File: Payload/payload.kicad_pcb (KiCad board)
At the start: 4 copper layers, 90 x 40 mm, 85 parts, among them J1 Conn_ARM_JTAG_SWD_10, J2 Conn_01x02, J3 Conn_01x03, Q1 Q_PMOS_GSD, SW1 SW_SPST, U1 STM32L471RGTx, U2 ISO1541, U3 MAX6371, U4 CY62167EV30LL, U5 CY62167EV30LL, U6 CY62167EV30LL, U7 CY62167EV30LL, Y1 8 MHz

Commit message: Partial routing
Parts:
- moved C13 1.25 mm to (127.2, 80.0)
- moved C14 1.25 mm to (102.2, 102.0)
- moved C15 1.25 mm to (127.2, 102.0)
- moved C9 1.25 mm to (102.2, 80.0)
- moved U4 1.25 mm to (114.2, 79.0)
- moved U5 1.25 mm to (139.2, 79.0)
- moved U6 1.25 mm to (114.2, 101.0)
- moved U7 1.25 mm to (139.2, 101.0)
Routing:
- net /A1: track 0.00 -> 126.9 mm, vias 0 -> 5
- net /A2: track 0.00 -> 125.6 mm, vias 0 -> 5
- net /A3: track 0.00 -> 123.2 mm, vias 0 -> 5
- net /A4: track 0.00 -> 120.5 mm, vias 0 -> 5
- net /A5: track 0.00 -> 117.7 mm, vias 0 -> 5
- net /A6: track 0.00 -> 114.7 mm, vias 0 -> 5
- net /A7: track 0.00 -> 111.9 mm, vias 0 -> 5
- net /A0: track 0.00 -> 110.8 mm, vias 0 -> 7
- net /A20: track 0.00 -> 110.7 mm, vias 0 -> 5
- net /A16: track 0.00 -> 110.0 mm, vias 0 -> 5
- net /A17: track 0.00 -> 109.1 mm, vias 0 -> 5
- net /A18: track 0.00 -> 106.7 mm, vias 0 -> 5
- net /A19: track 0.00 -> 106.3 mm, vias 0 -> 5
- net /A8: track 0.00 -> 103.0 mm, vias 0 -> 5
- net /A9: track 0.00 -> 100.0 mm, vias 0 -> 5
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
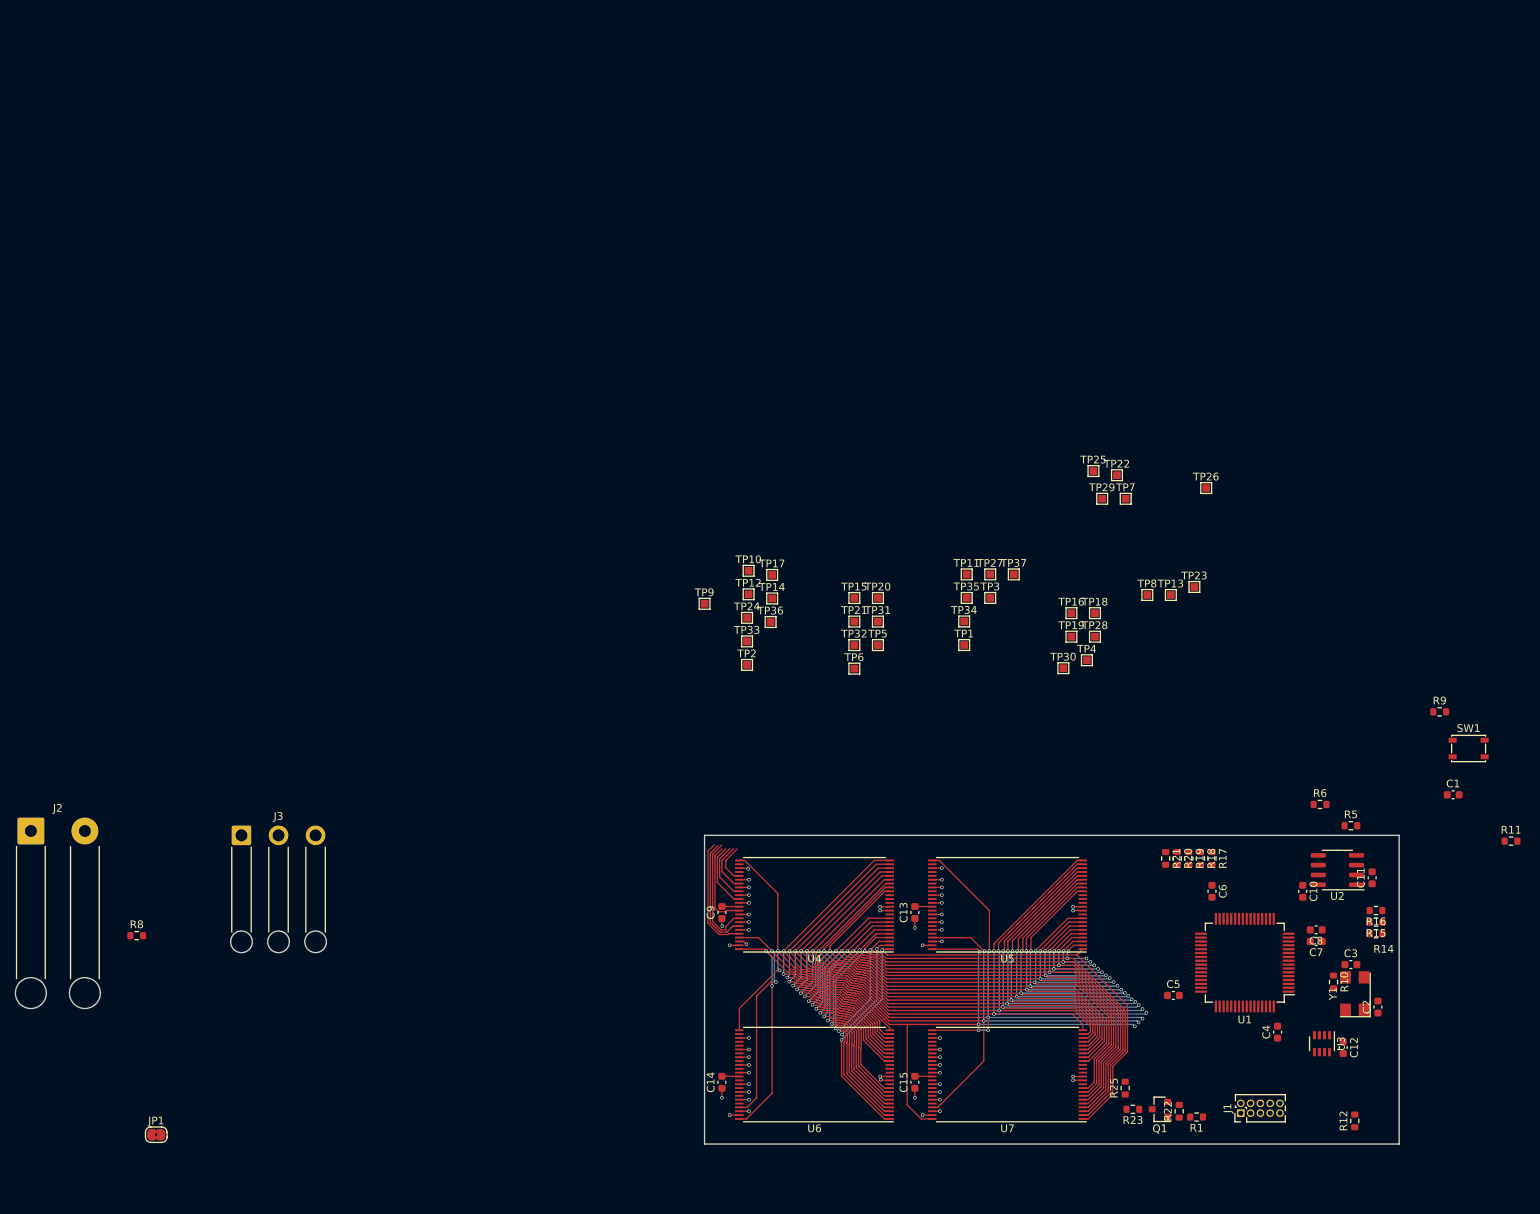
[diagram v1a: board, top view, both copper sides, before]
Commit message: Reduced BOM to fit, routed
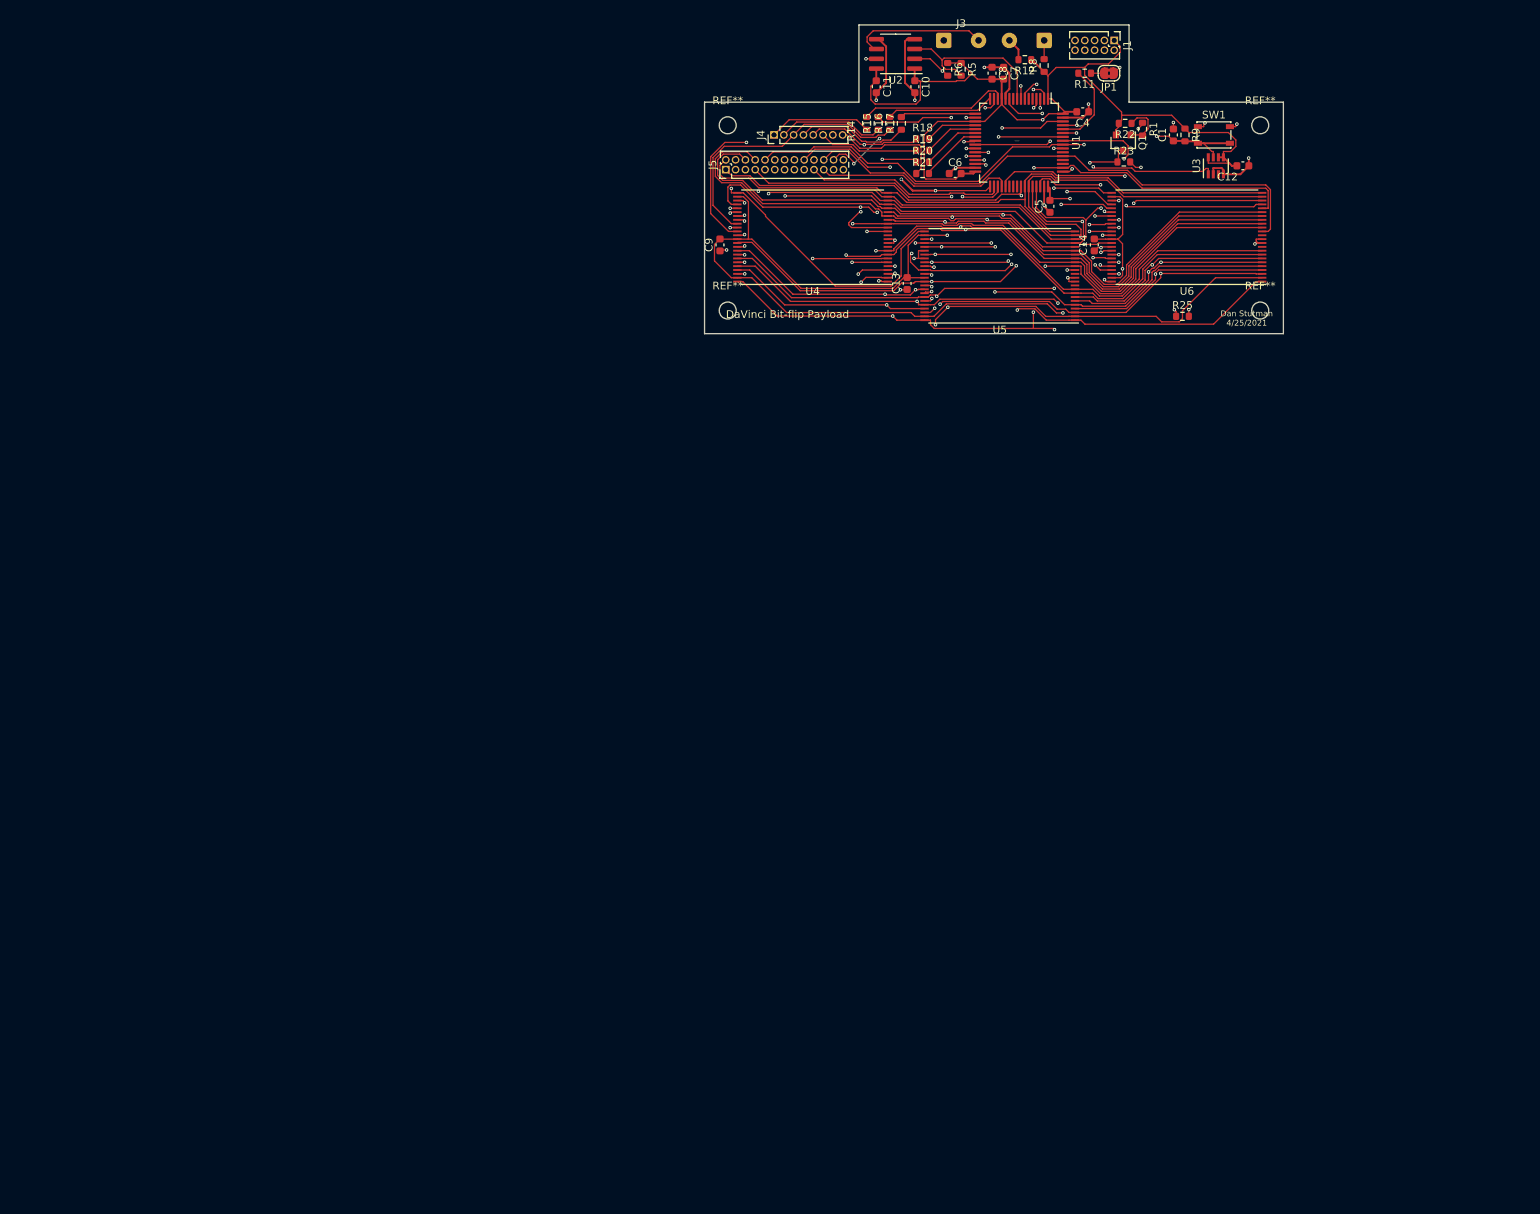
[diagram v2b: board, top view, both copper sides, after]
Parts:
- removed C15: 100 nF, Capacitor_SMD:C_0603_1608Metric
- removed C2, C3: C_Small, Capacitor_SMD:C_0603_1608Metric
- removed R10: R_Small_US, Resistor_SMD:R_0603_1608Metric
- removed TP1, TP10, TP11, TP12, TP13, TP14, TP15, TP16, TP17, TP18, TP19, TP2, TP20, TP21, TP22, TP23, TP24, TP25, TP26, TP27, TP28, TP29, TP3, TP30, TP31, TP32, TP33, TP34, TP35, TP36, TP37, TP4, TP5, TP6, TP7, TP8, TP9: TestPoint, TestPoint:TestPoint_Pad_1.0x1.0mm
- removed U7: CY62167EV30LL, Package_SO:TSOP-I-48_18.4x12mm_P0.5mm
- removed Y1: 8 MHz, Payload2:Crystal_SMD_DiodesIncorporated_FY
- added J4: Conn_01x08, Connector_PinHeader_1.27mm:PinHeader_1x08_P1.27mm_Vertical, F.Cu at (109.0, -20.8)
- added J5: Conn_02x13_Counter_Clockwise, Connector_PinHeader_1.27mm:PinHeader_2x13_P1.27mm_Vertical, F.Cu at (102.8, -16.2)
- added REF**: MountingHole_2.2mm_M2, MountingHole:MountingHole_2.2mm_M2, F.Cu at (172.0, -22.0)
- added REF**: MountingHole_2.2mm_M2, MountingHole:MountingHole_2.2mm_M2, F.Cu at (172.0, 2.00)
- added REF**: MountingHole_2.2mm_M2, MountingHole:MountingHole_2.2mm_M2, F.Cu at (103.0, 2.00)
- added REF**: MountingHole_2.2mm_M2, MountingHole:MountingHole_2.2mm_M2, F.Cu at (103.0, -22.0)
- J2: footprint Connector_Wire:SolderWire-0.75sqmm_1x02_P7mm_D1.25mm_OD3.5mm_Relief -> Connector_Wire:SolderWire-0.25sqmm_1x02_P4.5mm_D0.65mm_OD2mm; moved to B.Cu
- J3: value Conn_01x03 -> Conn_01x02; footprint Connector_Wire:SolderWire-0.75sqmm_1x03_P4.8mm_D1.25mm_OD2.3mm_Relief -> Connector_Wire:SolderWire-0.25sqmm_1x02_P4.5mm_D0.65mm_OD2mm
- moved JP1 184.8 mm to (152.4, -28.8), turned to 180 degrees
- moved J2 166.5 mm to (144.0, -33.0), turned to 180 degrees
- moved R8 162.9 mm to (144.0, -29.8), turned to 90 degrees
- moved R12 144.0 mm to (141.5, -30.5), turned to 180 degrees
- moved J1 140.0 mm to (153.1, -33.0), turned to 270 degrees
- moved J3 137.4 mm to (131.0, -33.0)
- moved R1 128.2 mm to (156.8, -21.5), turned to 270 degrees
- moved R22 128.2 mm to (154.5, -22.2), turned to 180 degrees
- moved Q1 125.3 mm to (154.2, -19.8), turned to 270 degrees
- moved R14 124.0 mm to (121.0, -22.2), turned to 90 degrees
- moved R23 122.8 mm to (154.3, -17.2), turned to 0 degrees
- moved R15 122.0 mm to (122.5, -22.2), turned to 90 degrees
- moved C4 121.9 mm to (149.0, -23.8), turned to 180 degrees
- moved C11 121.0 mm to (122.2, -27.0), turned to 270 degrees
- moved U2 120.3 mm to (124.8, -31.2)
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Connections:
- U1 pad 51: /M4_CE -> Net-(U1-Pad51)
- U1 pad 52: /M3_CE -> /M4_CE
- U1 pad 53: /M2_CE -> /M3_CE
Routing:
- net Net-(C13-Pad2): track 14.0 -> 168.5 mm, vias 4 -> 6
- net VCC: track 0.00 -> 144.5 mm, vias 0 -> 2
- net /~WE: track 0.00 -> 117.6 mm, vias 0 -> 3
- net /IO5: track 15.2 -> 103.1 mm, vias 0 -> 3
- net /IO1: track 6.46 -> 92.1 mm, vias 0 -> 4
- net /IO0: track 5.26 -> 90.5 mm, vias 0 -> 4
- net /IO3: track 8.55 -> 93.6 mm, vias 0 -> 4
- net /IO2: track 7.50 -> 92.5 mm, vias 0 -> 3
- net /~OE: track 0.00 -> 84.9 mm, vias 0 -> 6
- net /IO7: track 15.2 -> 94.9 mm, vias 0 -> 3
- net /IO4: track 11.5 -> 89.9 mm, vias 0 -> 4
- net /IO6: track 15.0 -> 86.6 mm, vias 0 -> 4
- net /M3_CE: track 0.00 -> 69.6 mm
- net /M2_CE: track 0.00 -> 49.6 mm, vias 0 -> 1
- net /NRST: track 0.00 -> 45.4 mm, vias 0 -> 2
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- removed copper zone on In1.Cu, net Net-(C13-Pad2)
- removed copper zone on In1.Cu, net VCC
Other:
- board size 90 x 40 mm -> 75 x 40 mm
- board text added: "DaVinci Bit-flip Payload"
- board text added: "Dan Stutman 4/25/2021"

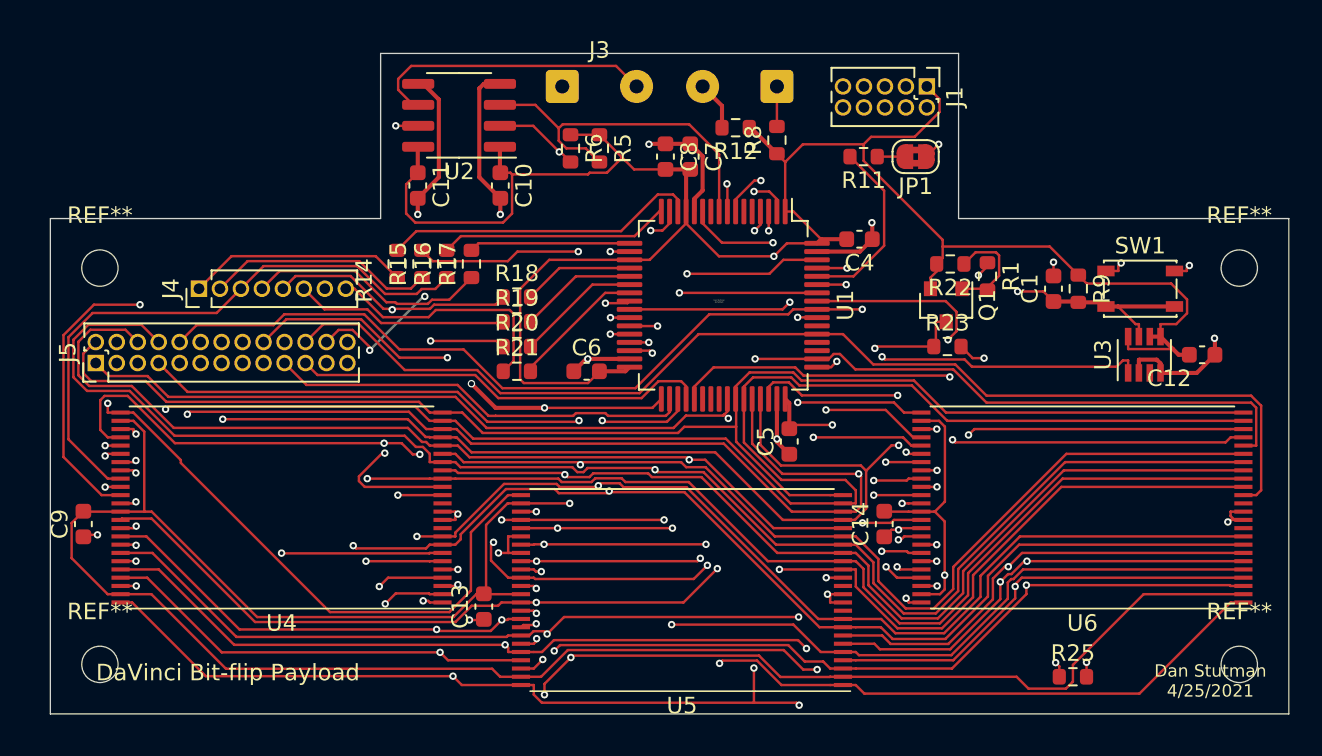
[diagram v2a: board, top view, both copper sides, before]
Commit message: Silk corrections and fix routes
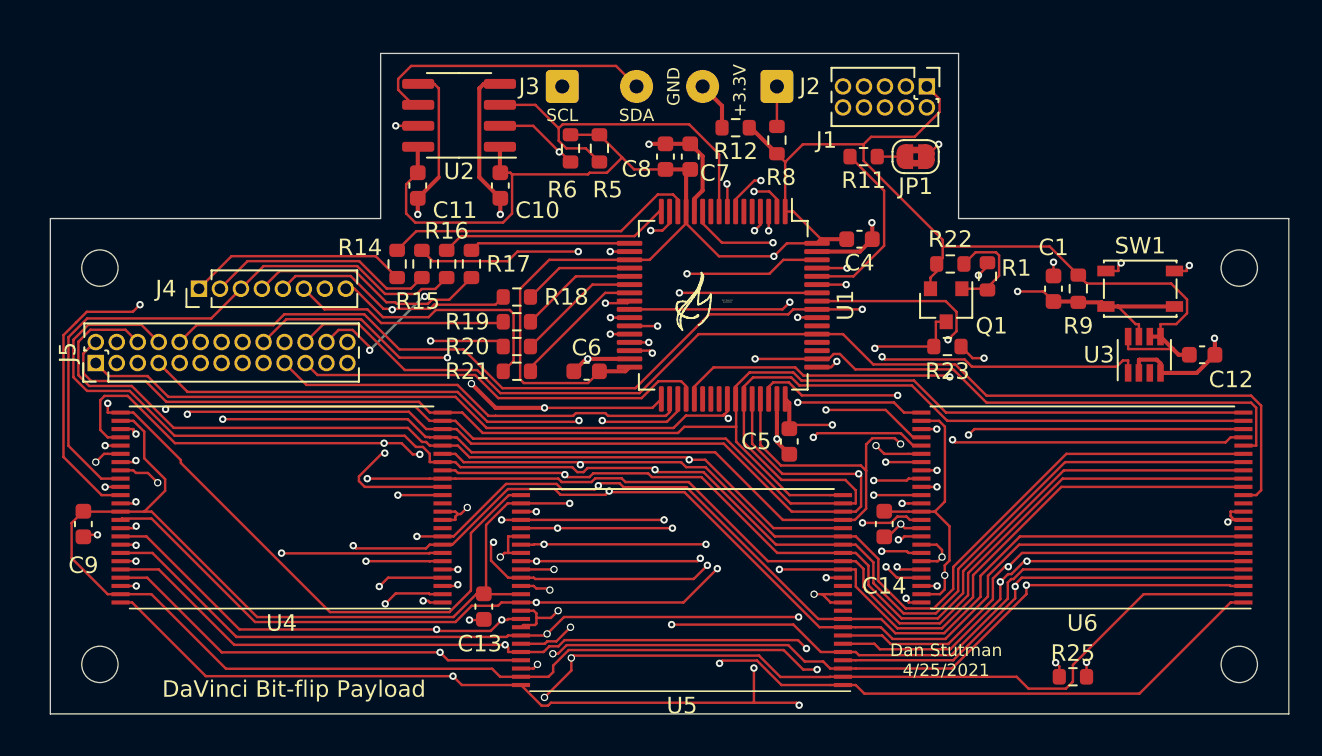
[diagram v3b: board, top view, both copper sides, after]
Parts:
- J2: moved to F.Cu
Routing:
- net GND: track 93.6 -> 107.3 mm, vias 44 -> 42
- net Net-(C13-Pad2): track 168.5 -> 170.0 mm
- net /A4: track 84.3 -> 85.5 mm
- net /~OE: track 84.9 -> 83.8 mm
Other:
- board text added: "+3.3V"
- board text added: "Flight Hardware Prototype"
- board text added: "GND"
- board text added: "SCL"
- board text added: "SDA"
